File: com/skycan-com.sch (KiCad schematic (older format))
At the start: 8 parts, among them J1 DF9_25P_1V_PLUG, J2 DF9_25P_1V_SOCKET, J3 DF9_25P_1V_PLUG, J4 DF9_25P_1V_SOCKET

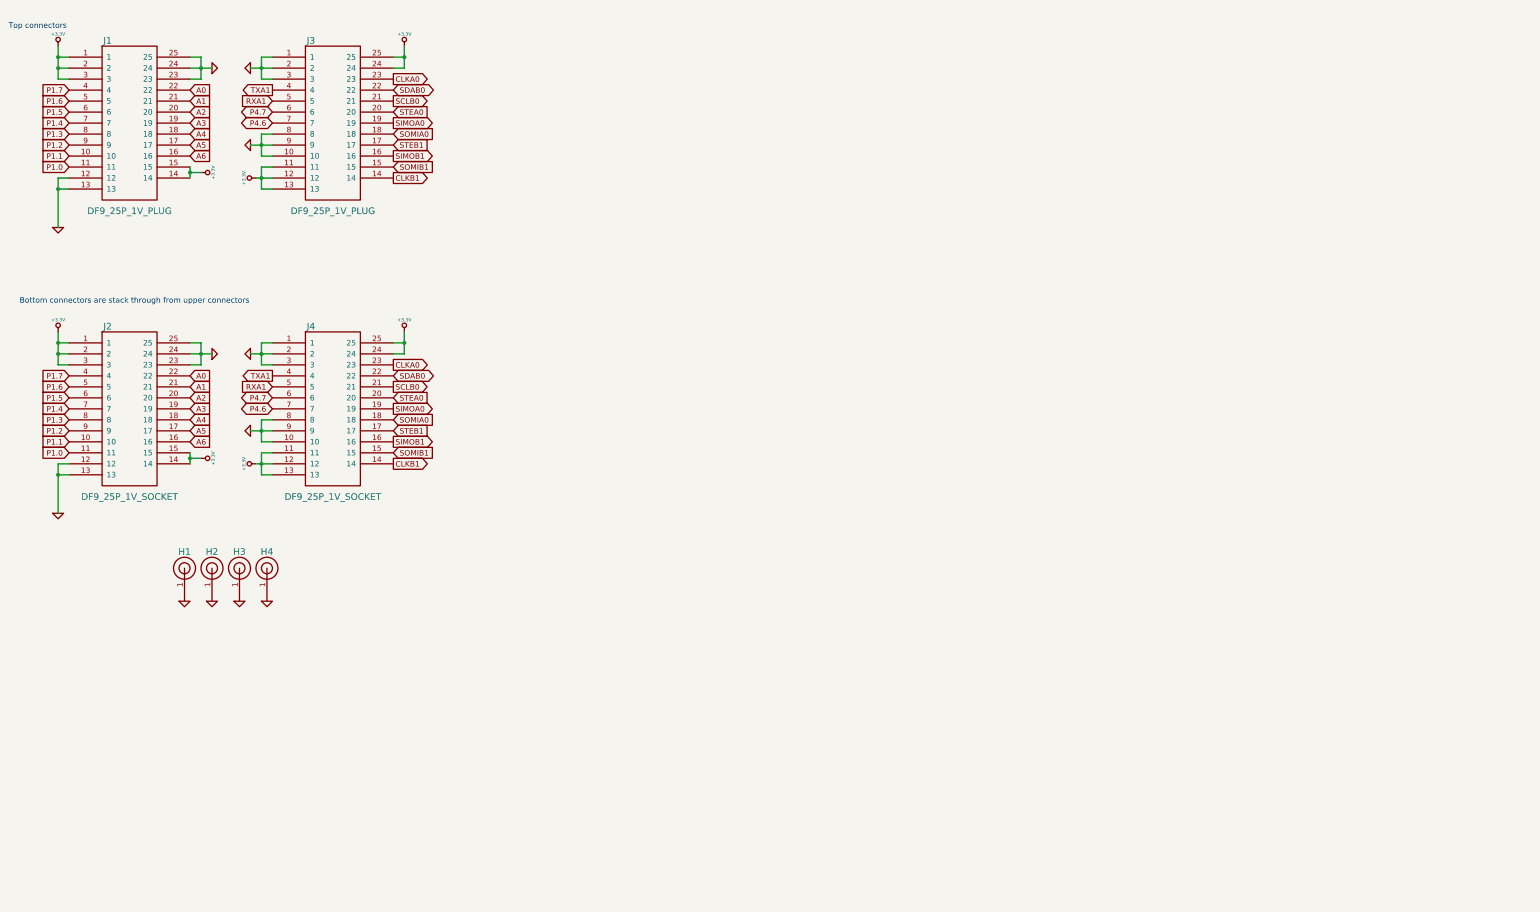
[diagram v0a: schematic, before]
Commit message: CC1120 with TCXO placed, matching is WIP
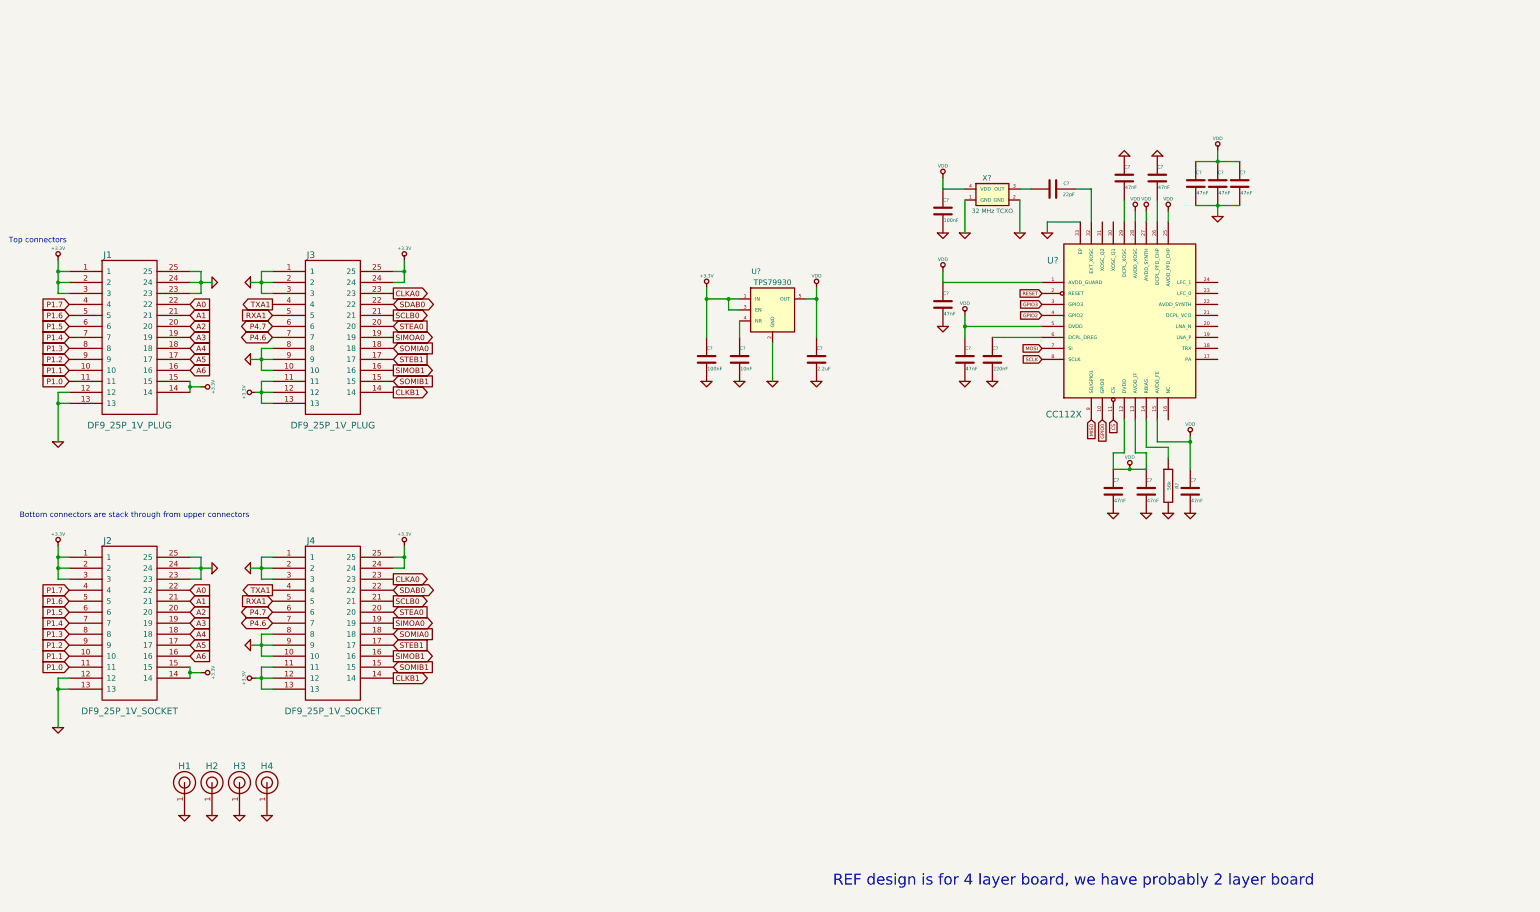
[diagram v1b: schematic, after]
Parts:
- added C? (x2): 100nF, 0402, symbol C
- added C?: 10nF, 0402, symbol C
- added C?: 2.2uF, 0805, symbol C
- added C? (x10): 47nF, 0402, symbol C
- added C?: 220nF, 0402, symbol C
- added C?: 22pF, 0402, symbol C
- added R?: 56k, 0402, symbol R
- added U?: CC112X, symbol CC112X
- added U?: TPS79930, symbol TPS79930
- added X?: 32 MHz TCXO, symbol WT325TCXO
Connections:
- net +3.3V: now also C?.1, U?.1 (IN), U?.3 (EN)
- net GND: now also C?.1, C?.1, C?.2, C?.2, C?.2, C?.2, C?.2, C?.2, C?.2, C?.2, C?.2, C?.2, C?.2, C?.2, C?.2, R?.2, U?.2 (GND), U?.33 (EP), X?.1 (GND), X?.2 (GND)
- new net: R?.1, U?.14 (RBIAS)
- new net: C?.2, U?.26 (DCPL_PFD_CHP)
- new net: C?.2, U?.29 (DCPL_XOSC)
- new net: C?.2, U?.32 (EXT_XOSC)
- new net: C?.1, U?.6 (DCPL_DREG)
- new net: C?.1, U?.4 (NR)
- new net: C?.1, X?.3 (OUT)
- new net CS: U?.11 (CS)
- new net GPIO0: U?.10 (GPIO0)
- new net GPIO2: U?.4 (GPIO2)
- new net GPIO3: U?.3 (GPIO3)
- new net MISO: U?.9 (SO/GPIO1)
- new net MOSI: U?.7 (SI)
- new net RESET: U?.2 (RESET)
- new net SCLK: U?.8 (SCLK)
- new net VDD: C?.1, C?.1, C?.1, C?.1, C?.1, C?.1, C?.1, C?.1, C?.1, C?.1, U?.1 (AVDD_GUARD), U?.12 (DVDD), U?.13 (AVDD_IF), U?.15 (AVDD_FE), U?.25 (AVDD_PFD_CHP), U?.27 (AVDD_SYNTH), U?.28 (AVDD_XOSC), U?.5 (DVDD), U?.5 (OUT), X?.4 (VDD)
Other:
- note added: "REF design is for 4 layer board, we have probably 2 layer board"
- moved on the sheet: H1, H2, H3, H4, J1, J2, J3, J4

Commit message: finish cc1120 schematic
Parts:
- added C?: 1.8nF, 0402, symbol C
- added C?: 47nF, 0402, symbol C
- added C? (x2): 10nF, 0402, symbol C
- added C? (x3): 5.1pF, 0402, symbol C
- added C?: 39pF, 0402, symbol C
- added C?: 2.2pF, 0402, symbol C
- added C?: NA, 0402, symbol C
- added C?: 6.2pF, 0402, symbol C
- added C?: 56pF, 0402, symbol C
- added C?: 100pF, 0402, symbol C
- added L? (x2): 56nH, symbol INDUCTOR_SMALL
- added L? (x2): 27nH, symbol INDUCTOR_SMALL
- added L? (x2): 15nH, symbol INDUCTOR_SMALL
- added L?: 43nH, symbol INDUCTOR_SMALL
- added L?: 22nH, symbol INDUCTOR_SMALL
- added R?: 18R, 0402, symbol R
- added U?: UFL, symbol UFL
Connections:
- net GND: now also C?.1, C?.1, C?.1, C?.2, C?.2, C?.2, L?.2, U?.2 (GND), U?.3 (GND)
- net VDD: now also U?.22 (AVDD_SYNTH), C?.1, C?.1, C?.2, C?.2, R?.2
- net at U?.17 (PA): now also C?.1, L?.2
- net at U?.18 (TRX): now also C?.2, L?.1
- net at U?.19 (LNA_P): now also C?.1, L?.1, L?.1
- net at U?.20 (LNA_N): now also C?.1, L?.1, L?.2
- net at U?.21 (DCPL_VCO): now also C?.1
- net at U?.23 (LFC_0): now also C?.2
- net at U?.24 (LFC_1): now also C?.1
- new net: C?.2, L?.2, L?.2
- new net: C?.1, C?.2, L?.1
- new net: C?.1, C?.2, L?.1, L?.2 (x2)
- new net: C?.2, L?.2, U?.1 (S)
- new net: C?.2, L?.1, R?.1
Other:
- moved on the sheet: C?, R?, U?, X?

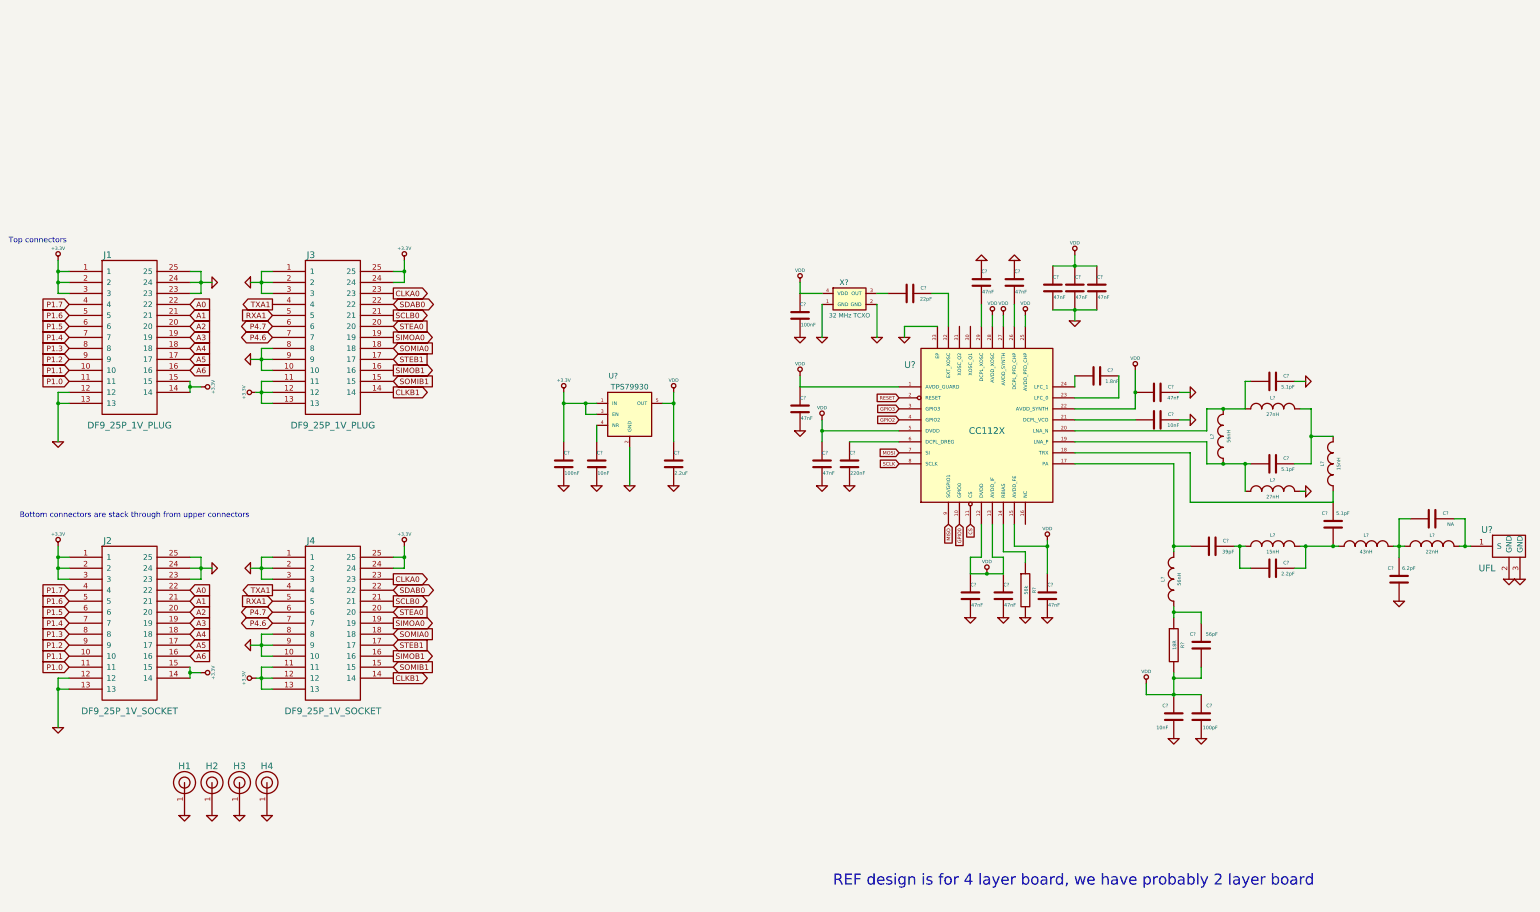
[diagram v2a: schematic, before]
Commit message: add NRF8001, Johanson balun and chip antenna to COM schematic
schematic is now ready
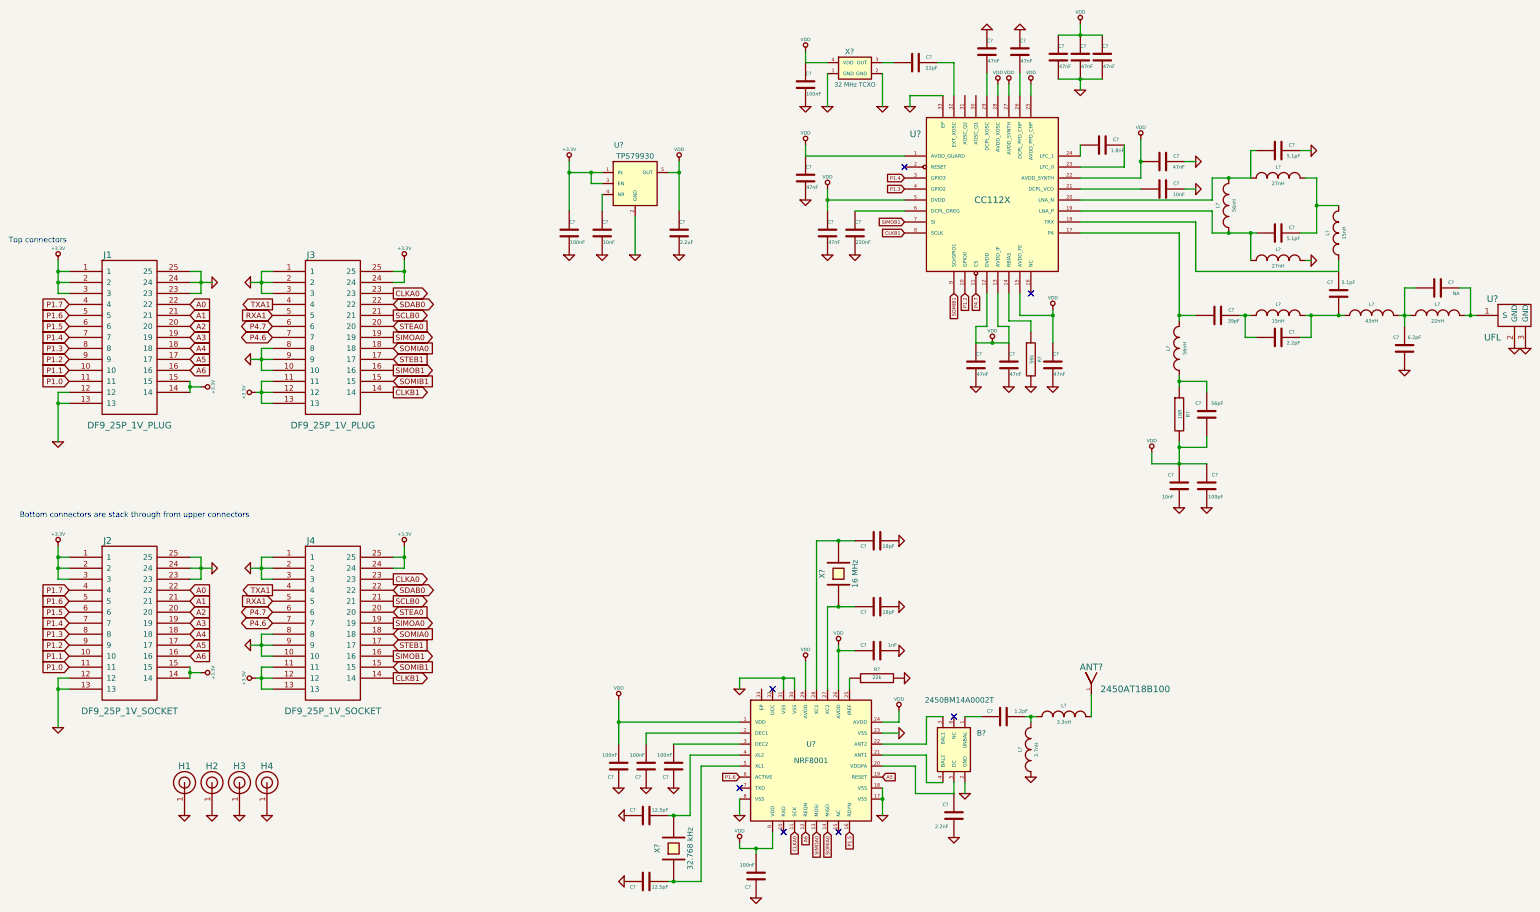
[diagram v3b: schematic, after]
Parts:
- added ANT?: 2450AT18B100, symbol 2450AT18B100
- added B?: 2450BM14A0002T, symbol 2450BM14A0002T
- added C?: 2.2nF, 0402, symbol C
- added C? (x2): 18pF, 0402, symbol C
- added C?: 1nF, 0402, symbol C
- added C? (x4): 100nF, 0402, symbol C
- added C? (x2): 12.5pF, 0402, symbol C
- added C?: 1.2pF, 0402, symbol C
- added L?: 3.3nH, symbol INDUCTOR_SMALL
- added L?: 2.7nH, symbol INDUCTOR_SMALL
- added R?: 22k, 0402, symbol R
- added U?: NRF8001, symbol NRF8001
- added X?: 16 MHz, symbol CRYSTAL
- added X?: 32.768 kHz, symbol CRYSTAL
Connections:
- net CS is gone; now on net P4.7: U?.11 (CS)
- net GPIO0 is gone; now on net P1.2: U?.10 (GPIO0)
- net GPIO2 is gone; now on net P1.3: U?.4 (GPIO2)
- net GPIO3 is gone; now on net P1.4: U?.3 (GPIO3)
- net MISO is gone; now on net SOMIB1: U?.9 (SO/GPIO1)
- net MOSI is gone; now on net SIMOB1: U?.7 (SI)
- net SCLK is gone; now on net CLKB1: U?.8 (SCLK)
- net A5: now also U?.19 (RESET)
- net A6: now also U?.12 (REQN)
- net CLKA0: now also U?.11 (SCK)
- net GND: now also B?.2 (GND), C?.1, C?.1, C?.1, C?.1, C?.2, C?.2, C?.2, C?.2, C?.2, C?.2, L?.1, R?.2, U?.17 (VSS), U?.18 (VSS), U?.23 (VSS), U?.30 (VSS), U?.31 (VSS), U?.8 (VSS)
- net P1.5: now also U?.16 (RDYN)
- net P1.6: now also U?.6 (ACTIVE)
- net SIMOA0: now also U?.13 (MOSI)
- net SOMIA0: now also U?.14 (MISO)
- net VDD: now also C?.1, C?.1, C?.2, U?.1 (VDD), U?.24 (AVDD), U?.26 (AVDD), U?.29 (AVDD), U?.9 (VDD)
- net RESET: no longer names the net of U?.2 (RESET)
- new net: C?.1, U?.2 (DEC1)
- new net: B?.5 (DC), C?.2, U?.20 (VDDPA)
- new net: B?.4 (BAL2), U?.21 (ANT1)
- new net: B?.3 (BAL1), U?.22 (ANT2)
- new net: R?.1, U?.25 (IREF)
- new net: C?.2, U?.27 (XC2), X?.1
- new net: C?.2, U?.28 (XC1), X?.2
- new net: C?.1, U?.3 (DEC2)
- new net: C?.1, U?.4 (XL2), X?.2
- new net: C?.1, U?.5 (XL1), X?.1
- new net: B?.1 (UNBAL), C?.2
- new net: ANT?.1, L?.2
- new net: C?.1, L?.1, L?.2
- no-connect marks 0 -> 7
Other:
- note removed: "REF design is for 4 layer board, we have probably 2 layer board"
- moved on the sheet: C?, L?, R?, U?, X?

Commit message: generate nets and assigne footprins
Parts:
- removed U?: NRF8001, symbol NRF8001
- added U2: NRF8001, symbol NRF8001
- gave numbers to parts that had none: 61
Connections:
- net A5: now also U2.19 (RESET)
- net A6: now also U2.12 (REQN)
- net CLKA0: now also U2.11 (SCK)
- net GND: now also U2.17 (VSS), U2.18 (VSS), U2.23 (VSS), U2.30 (VSS), U2.31 (VSS), U2.33 (EP), U2.8 (VSS)
- net P1.5: now also U2.16 (RDYN)
- net P1.6: now also U2.6 (ACTIVE)
- net SIMOA0: now also U2.13 (MOSI)
- net SOMIA0: now also U2.14 (MISO)
- net VDD: now also U2.1 (VDD), U2.24 (AVDD), U2.26 (AVDD), U2.29 (AVDD), U2.9 (VDD)
- net at C4.1: now also U2.2 (DEC1)
- net at B1.5 (DC), C18.2: now also U2.20 (VDDPA)
- net at B1.4 (BAL2): now also U2.21 (ANT1)
- net at B1.3 (BAL1): now also U2.22 (ANT2)
- net at R1.1: now also U2.25 (IREF)
- net at C15.2, X2.1: now also U2.27 (XC2)
- net at C14.2, X2.2: now also U2.28 (XC1)
- net at C7.1: now also U2.3 (DEC2)
- net at C5.1, X1.2: now also U2.4 (XL2)
- net at C6.1, X1.1: now also U2.5 (XL1)
- no-connect marks 7 -> 9
